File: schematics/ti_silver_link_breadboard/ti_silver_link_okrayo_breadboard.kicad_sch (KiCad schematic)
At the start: 35 parts, among them P1 USB_B, U1 24LC256, U2 MCP17003302E, U3 TUSB3410, U4A PN2222A, U4B PN2222A, Y1 12MHz

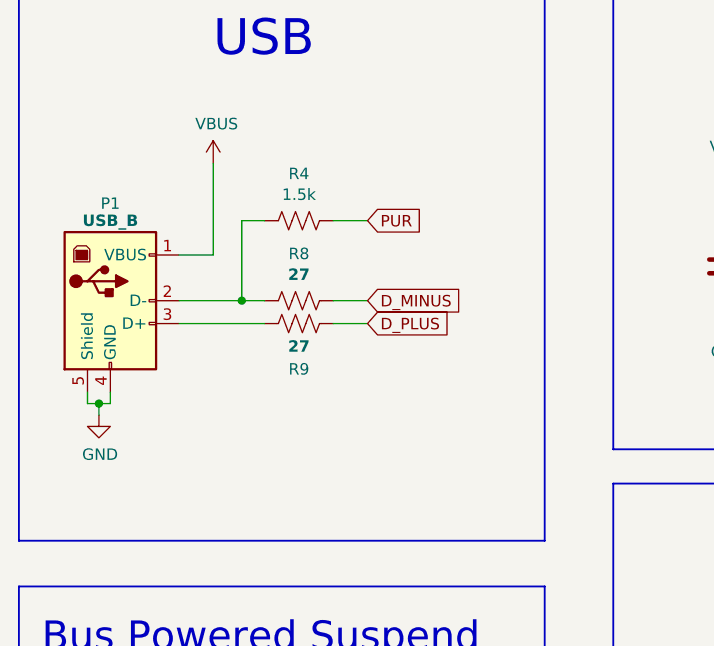
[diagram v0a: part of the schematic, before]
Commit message: Correct "B" and "okrayo" PUR resistor connection to D+
Rev 1 schematic incorrectly identified PUR resistor connection to D- and
had the series resistors for D+/D- (R8/R9) swapped. Move PUR resistor R4
to D+ and use R8 for D+ and R9 for D-.
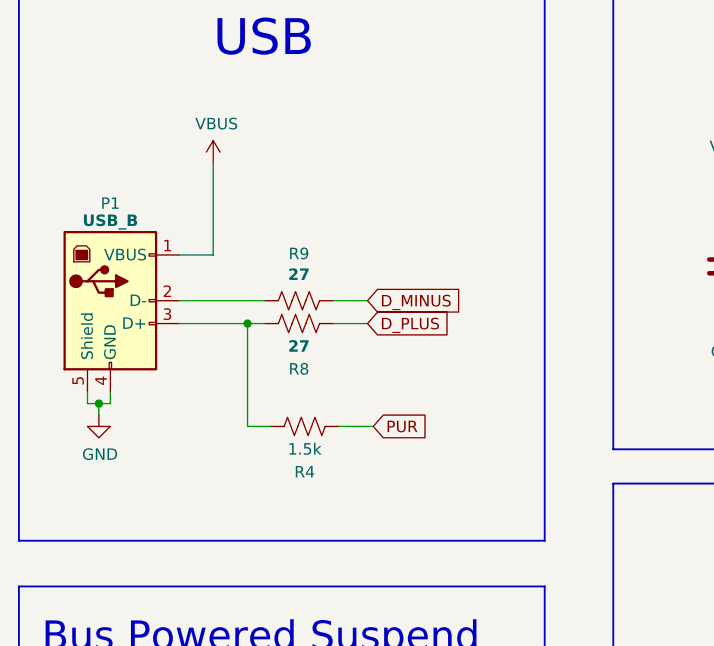
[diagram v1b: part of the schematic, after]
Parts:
- renumbered R9 to R8, R8 to R9
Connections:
- net at P1.2 (D-), R9.2: no longer R4.2
- net at P1.3 (D+), R8.2: now also R4.2
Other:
- moved on the sheet: R4
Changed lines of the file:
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@@
   (title_block
     (title "TI USB Graph Link \"okrayo\" Breadboard")
-    (date "2023-Jun-17")
-    (rev "1")
+    (date "2023-Jul-09")
+    (rev "2")
   )
   (junction (at 114.3 139.7) (diameter 0) (color 0 0 0 0)
@@
   (junction (at 135.89 44.45) (diameter 0) (color 0 0 0 0)
   )
+  (junction (at 60.96 57.15) (diameter 0) (color 0 0 0 0)
+  )
   (junction (at 44.45 66.04) (diameter 0) (color 0 0 0 0)
-  )
-  (junction (at 60.325 54.61) (diameter 0) (color 0 0 0 0)
   )
   (junction (at 64.77 118.11) (diameter 0) (color 0 0 0 0)
@@
     (stroke (width 0.2032) (type solid))
   )
-  (wire (pts (xy 70.485 45.72) (xy 74.295 45.72))
-    (stroke (width 0) (type default))
-  )
   (wire (pts (xy 233.68 83.82) (xy 233.68 85.09))
     (stroke (width 0) (type default))
@@
     (stroke (width 0) (type default))
   )
-  (wire (pts (xy 53.34 54.61) (xy 60.325 54.61))
+  (wire (pts (xy 53.34 54.61) (xy 62.865 54.61))
     (stroke (width 0) (type default))
   )
@@
     (stroke (width 0) (type default))
   )
-  (wire (pts (xy 60.325 45.72) (xy 60.325 54.61))
-    (stroke (width 0) (type default))
-  )
   (wire (pts (xy 135.89 54.61) (xy 135.89 55.88))
     (stroke (width 0) (type default))
@@
     (stroke (width 0) (type default))
   )
+  (wire (pts (xy 60.96 57.15) (xy 60.96 68.58))
+    (stroke (width 0) (type default))
+  )
   (wire (pts (xy 237.49 60.96) (xy 238.76 60.96))
     (stroke (width 0) (type default))
@@
     (stroke (width 0) (type default))
   )
-  (wire (pts (xy 60.325 54.61) (xy 62.865 54.61))
-    (stroke (width 0) (type default))
-  )
   (wire (pts (xy 154.94 40.64) (xy 154.94 39.37))
     (stroke (width 0) (type default))
@@
     (stroke (width 0.2032) (type solid))
   )
-  (wire (pts (xy 62.865 45.72) (xy 60.325 45.72))
+  (wire (pts (xy 63.5 68.58) (xy 60.96 68.58))
     (stroke (width 0) (type default))
   )
@@
     (stroke (width 0.2032) (type solid))
   )
+  (wire (pts (xy 60.96 57.15) (xy 62.865 57.15))
+    (stroke (width 0) (type default))
+  )
   (wire (pts (xy 70.485 57.15) (xy 74.295 57.15))
     (stroke (width 0) (type default))
@@
     (stroke (width 0) (type default))
   )
-  (wire (pts (xy 53.34 57.15) (xy 62.865 57.15))
+  (wire (pts (xy 53.34 57.15) (xy 60.96 57.15))
     (stroke (width 0) (type default))
   )
@@
   )
   (wire (pts (xy 154.94 92.71) (xy 154.94 91.44))
+    (stroke (width 0) (type default))
+  )
+  (wire (pts (xy 71.12 68.58) (xy 74.93 68.58))
     (stroke (width 0) (type default))
   )
@@
     )
   )
-  (global_label "PUR" (shape input) (at 74.295 45.72 0)
-    (effects (font (size 1.27 1.27)) (justify left))
-    (property "Intersheetrefs" "${INTERSHEET_REFS}" (at 74.295 45.72 0)
+  (global_label "PUR" (shape input) (at 74.93 68.58 0)
+    (effects (font (size 1.27 1.27)) (justify left))
+    (property "Intersheetrefs" "${INTERSHEET_REFS}" (at 74.93 68.58 0)
       (effects (font (size 1.27 1.27)) hide)
     )
@@
   (symbol (lib_id "Device:R_US") (at 66.675 54.61 270) (unit 1)
     (in_bom yes) (on_board yes) (dnp no)
-    (property "Reference" "R8" (at 66.675 49.403 90)
+    (property "Reference" "R9" (at 66.675 49.403 90)
       (effects (font (size 1.27 1.27)))
     )
@@
     )
     (property "Datasheet" "~" (at 66.675 54.61 0)
+      (effects (font (size 1.27 1.27)) hide)
+    )
+    (pin "1")
+    (pin "2")
+    (instances
+      (project "ti_silver_link_okrayo_breadboard"
+        (path "/683ce4bc-ff39-4a7c-bc2d-3e6ddc8eca85"
+          (reference "R9") (unit 1)
+        )
+      )
+    )
+  )
+  (symbol (lib_id "Device:R_US") (at 66.675 57.15 270) (unit 1)
+    (in_bom yes) (on_board yes) (dnp no)
+    (property "Reference" "R8" (at 66.675 62.23 90)
+      (effects (font (size 1.27 1.27)))
+    )
+    (property "Value" "27" (at 66.675 59.69 90)
+      (effects (font (size 1.27 1.27) bold))
+    )
+    (property "Footprint" "" (at 66.421 58.166 90)
+      (effects (font (size 1.27 1.27)) hide)
+    )
+    (property "Datasheet" "~" (at 66.675 57.15 0)
       (effects (font (size 1.27 1.27)) hide)
     )
@@
     )
   )
-  (symbol (lib_id "Device:R_US") (at 66.675 57.15 270) (unit 1)
-    (in_bom yes) (on_board yes) (dnp no)
-    (property "Reference" "R9" (at 66.675 62.23 90)
-      (effects (font (size 1.27 1.27)))
-    )
-    (property "Value" "27" (at 66.675 59.69 90)
-      (effects (font (size 1.27 1.27) bold))
-    )
-    (property "Footprint" "" (at 66.421 58.166 90)
-      (effects (font (size 1.27 1.27)) hide)
-    )
-    (property "Datasheet" "~" (at 66.675 57.15 0)
-      (effects (font (size 1.27 1.27)) hide)
-    )
-    (pin "1")
-    (pin "2")
-    (instances
-      (project "ti_silver_link_okrayo_breadboard"
-        (path "/683ce4bc-ff39-4a7c-bc2d-3e6ddc8eca85"
-          (reference "R9") (unit 1)
-        )
-      )
-    )
-  )
   (symbol (lib_id "Device:C") (at 135.89 50.8 0) (unit 1)
     (in_bom yes) (on_board yes) (dnp no)
@@
     )
   )
-  (symbol (lib_id "Device:R_US") (at 66.675 45.72 270) (unit 1)
-    (in_bom yes) (on_board yes) (dnp no)
-    (property "Reference" "R4" (at 66.675 40.513 90)
-      (effects (font (size 1.27 1.27)))
-    )
-    (property "Value" "1.5k" (at 66.675 42.8244 90)
-      (effects (font (size 1.27 1.27)))
-    )
-    (property "Footprint" "" (at 66.421 46.736 90)
-      (effects (font (size 1.27 1.27)) hide)
-    )
-    (property "Datasheet" "~" (at 66.675 45.72 0)
-      (effects (font (size 1.27 1.27)) hide)
-    )
+  (symbol (lib_id "Device:R_US") (at 67.31 68.58 270) (unit 1)
+    (in_bom yes) (on_board yes) (dnp no)
+    (property "Reference" "R4" (at 67.31 73.66 90)
+      (effects (font (size 1.27 1.27)))
+    )
+    (property "Value" "1.5k" (at 67.31 71.12 90)
+      (effects (font (size 1.27 1.27)))
+    )
+    (property "Footprint" "" (at 67.056 69.596 90)
+      (effects (font (size 1.27 1.27)) hide)
+    )
+    (property "Datasheet" "~" (at 67.31 68.58 0)
+      (effects (font (size 1.27 1.27)) hide)
+    )

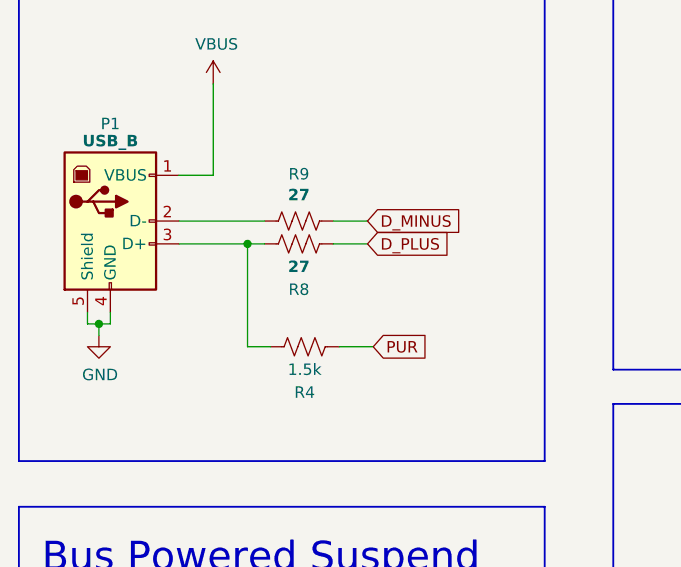
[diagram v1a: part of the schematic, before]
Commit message: Breadboard: move R4 D+ pullup resistor after R8 series resistor
TUSB3410 datasheet lists 1.5kΩ PUR pullup resistor after the D+ series
resistor. The USB Graph Link "B" schematic has this before the series
resistor. Correct "okrayo" breadboard schematic with this change to
align it with the datasheet.
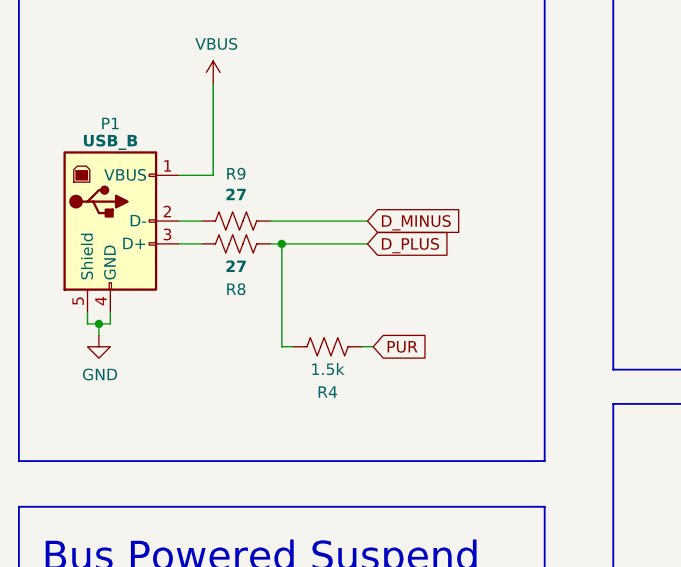
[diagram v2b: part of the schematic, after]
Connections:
- net D_PLUS: now also R4.2
- net at P1.3 (D+), R8.2: no longer R4.2
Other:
- moved on the sheet: R4, R8, R9
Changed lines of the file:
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@@
   (junction (at 238.76 60.96) (diameter 0) (color 0 0 0 0)
   )
+  (junction (at 64.77 57.15) (diameter 0) (color 0 0 0 0)
+  )
   (junction (at 215.9 127.635) (diameter 0) (color 0 0 0 0)
   )
@@
   )
   (junction (at 135.89 44.45) (diameter 0) (color 0 0 0 0)
-  )
-  (junction (at 60.96 57.15) (diameter 0) (color 0 0 0 0)
   )
   (junction (at 44.45 66.04) (diameter 0) (color 0 0 0 0)
@@
   (no_connect (at 175.26 132.08))
   (no_connect (at 175.26 124.46))
-  (wire (pts (xy 70.485 54.61) (xy 74.295 54.61))
+  (wire (pts (xy 63.5 54.61) (xy 74.295 54.61))
     (stroke (width 0) (type default))
   )
@@
     (stroke (width 0) (type default))
   )
+  (wire (pts (xy 64.77 57.15) (xy 74.295 57.15))
+    (stroke (width 0) (type default))
+  )
+  (wire (pts (xy 64.77 68.58) (xy 66.04 68.58))
+    (stroke (width 0) (type default))
+  )
   (wire (pts (xy 64.77 119.38) (xy 64.77 118.11))
     (stroke (width 0) (type default))
@@
     (stroke (width 0) (type default))
   )
+  (wire (pts (xy 64.77 57.15) (xy 64.77 68.58))
+    (stroke (width 0) (type default))
+  )
   (polyline (pts (xy 35.56 177.8) (xy 35.56 142.24))
     (stroke (width 0.2032) (type solid))
@@
     (stroke (width 0) (type default))
   )
-  (wire (pts (xy 53.34 54.61) (xy 62.865 54.61))
+  (wire (pts (xy 53.34 54.61) (xy 55.88 54.61))
     (stroke (width 0) (type default))
   )
@@
     (stroke (width 0) (type default))
   )
-  (wire (pts (xy 60.96 57.15) (xy 60.96 68.58))
-    (stroke (width 0) (type default))
-  )
   (wire (pts (xy 237.49 60.96) (xy 238.76 60.96))
     (stroke (width 0) (type default))
@@
     (stroke (width 0.2032) (type solid))
   )
-  (wire (pts (xy 63.5 68.58) (xy 60.96 68.58))
-    (stroke (width 0) (type default))
-  )
   (wire (pts (xy 217.17 125.095) (xy 215.9 125.095))
     (stroke (width 0) (type default))
@@
     (stroke (width 0.2032) (type solid))
   )
-  (wire (pts (xy 60.96 57.15) (xy 62.865 57.15))
-    (stroke (width 0) (type default))
-  )
-  (wire (pts (xy 70.485 57.15) (xy 74.295 57.15))
+  (wire (pts (xy 63.5 57.15) (xy 64.77 57.15))
     (stroke (width 0) (type default))
   )
@@
     (stroke (width 0) (type default))
   )
-  (wire (pts (xy 53.34 57.15) (xy 60.96 57.15))
+  (wire (pts (xy 53.34 57.15) (xy 55.88 57.15))
     (stroke (width 0) (type default))
   )
@@
     (stroke (width 0) (type default))
   )
-  (wire (pts (xy 71.12 68.58) (xy 74.93 68.58))
+  (wire (pts (xy 73.66 68.58) (xy 74.93 68.58))
     (stroke (width 0) (type default))
   )
@@
     )
   )
-  (symbol (lib_id "Device:R_US") (at 66.675 54.61 270) (unit 1)
-    (in_bom yes) (on_board yes) (dnp no)
-    (property "Reference" "R9" (at 66.675 49.403 90)
-      (effects (font (size 1.27 1.27)))
-    )
-    (property "Value" "27" (at 66.675 51.7144 90)
+  (symbol (lib_id "Device:R_US") (at 59.69 54.61 270) (unit 1)
+    (in_bom yes) (on_board yes) (dnp no)
+    (property "Reference" "R9" (at 59.69 49.403 90)
+      (effects (font (size 1.27 1.27)))
+    )
+    (property "Value" "27" (at 59.69 51.7144 90)
       (effects (font (size 1.27 1.27) bold))
     )
-    (property "Footprint" "" (at 66.421 55.626 90)
-      (effects (font (size 1.27 1.27)) hide)
-    )
-    (property "Datasheet" "~" (at 66.675 54.61 0)
+    (property "Footprint" "" (at 59.436 55.626 90)
+      (effects (font (size 1.27 1.27)) hide)
+    )
+    (property "Datasheet" "~" (at 59.69 54.61 0)
       (effects (font (size 1.27 1.27)) hide)
     )
@@
     )
   )
-  (symbol (lib_id "Device:R_US") (at 66.675 57.15 270) (unit 1)
-    (in_bom yes) (on_board yes) (dnp no)
-    (property "Reference" "R8" (at 66.675 62.23 90)
-      (effects (font (size 1.27 1.27)))
-    )
-    (property "Value" "27" (at 66.675 59.69 90)
+  (symbol (lib_id "Device:R_US") (at 59.69 57.15 270) (unit 1)
+    (in_bom yes) (on_board yes) (dnp no)
+    (property "Reference" "R8" (at 59.69 62.23 90)
+      (effects (font (size 1.27 1.27)))
+    )
+    (property "Value" "27" (at 59.69 59.69 90)
       (effects (font (size 1.27 1.27) bold))
     )
-    (property "Footprint" "" (at 66.421 58.166 90)
-      (effects (font (size 1.27 1.27)) hide)
-    )
-    (property "Datasheet" "~" (at 66.675 57.15 0)
+    (property "Footprint" "" (at 59.436 58.166 90)
+      (effects (font (size 1.27 1.27)) hide)
+    )
+    (property "Datasheet" "~" (at 59.69 57.15 0)
       (effects (font (size 1.27 1.27)) hide)
     )
@@
     )
   )
-  (symbol (lib_id "Device:R_US") (at 67.31 68.58 270) (unit 1)
-    (in_bom yes) (on_board yes) (dnp no)
-    (property "Reference" "R4" (at 67.31 73.66 90)
-      (effects (font (size 1.27 1.27)))
-    )
-    (property "Value" "1.5k" (at 67.31 71.12 90)
-      (effects (font (size 1.27 1.27)))
-    )
-    (property "Footprint" "" (at 67.056 69.596 90)
-      (effects (font (size 1.27 1.27)) hide)
-    )
-    (property "Datasheet" "~" (at 67.31 68.58 0)
-      (effects (font (size 1.27 1.27)) hide)
-    )
+  (symbol (lib_id "Device:R_US") (at 69.85 68.58 270) (unit 1)
+    (in_bom yes) (on_board yes) (dnp no)
+    (property "Reference" "R4" (at 69.85 73.66 90)
+      (effects (font (size 1.27 1.27)))
+    )
+    (property "Value" "1.5k" (at 69.85 71.12 90)
+      (effects (font (size 1.27 1.27)))
+    )
+    (property "Footprint" "" (at 69.596 69.596 90)
+      (effects (font (size 1.27 1.27)) hide)
+    )
+    (property "Datasheet" "~" (at 69.85 68.58 0)
+      (effects (font (size 1.27 1.27)) hide)
+    )

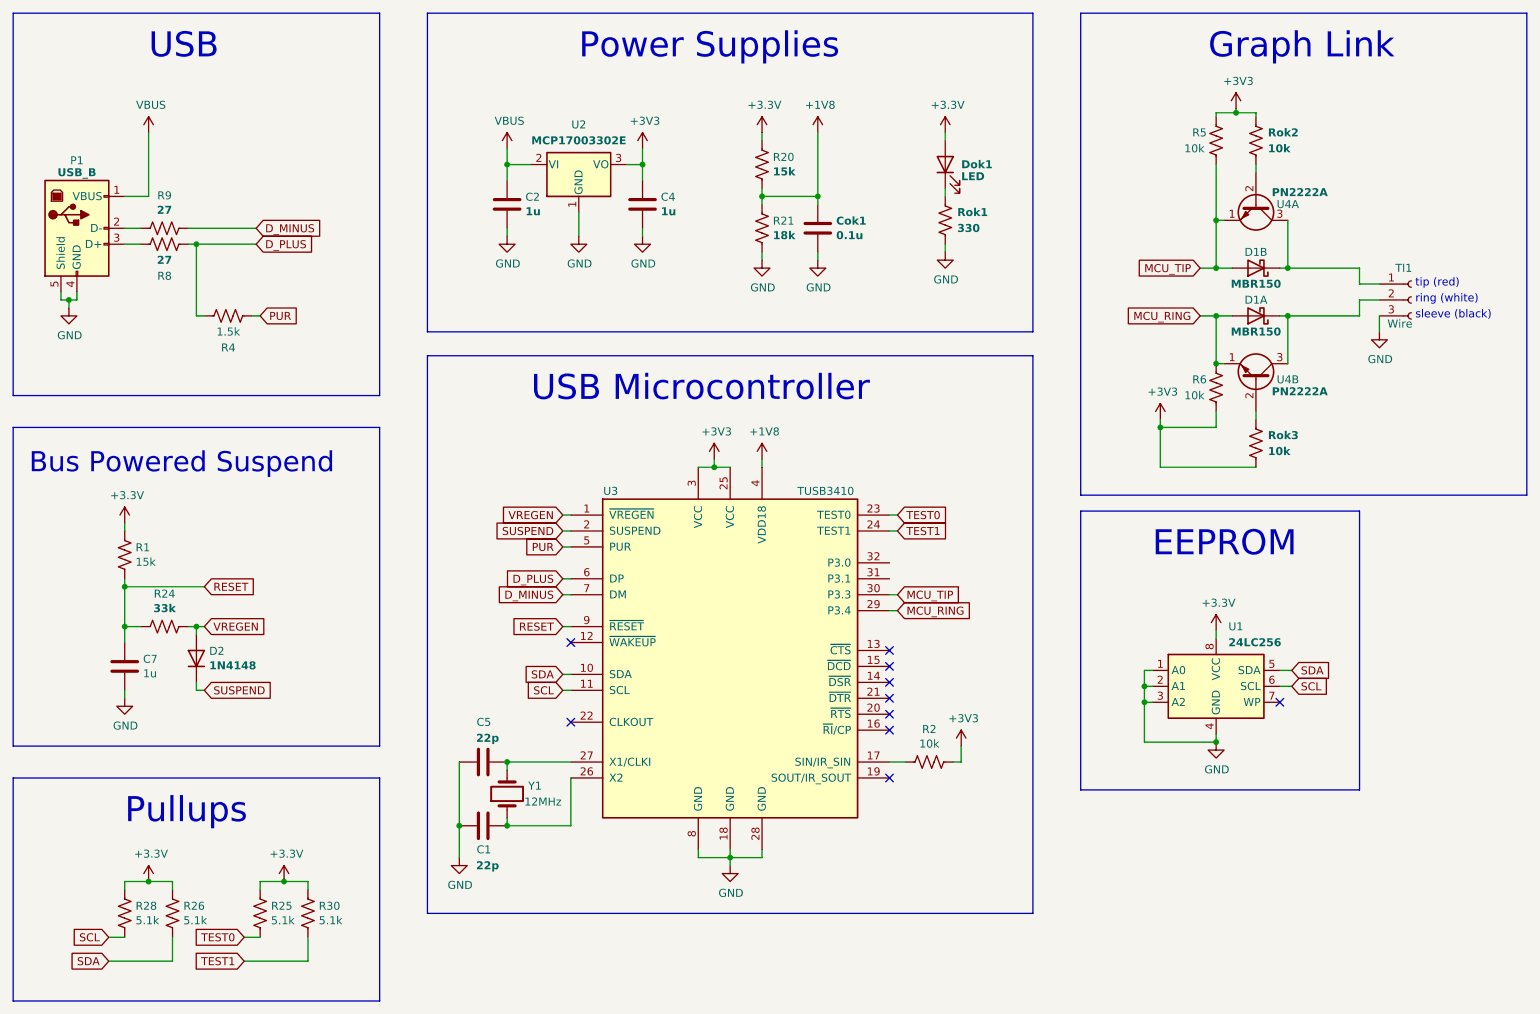
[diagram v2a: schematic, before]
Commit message: Convert all +3.3V nest to +3V3 in TI Silver Link "B" schematic
Addresses issue #3
USB Silver Link "B" schematic had a mix of +3.3V and +3V3 nets.
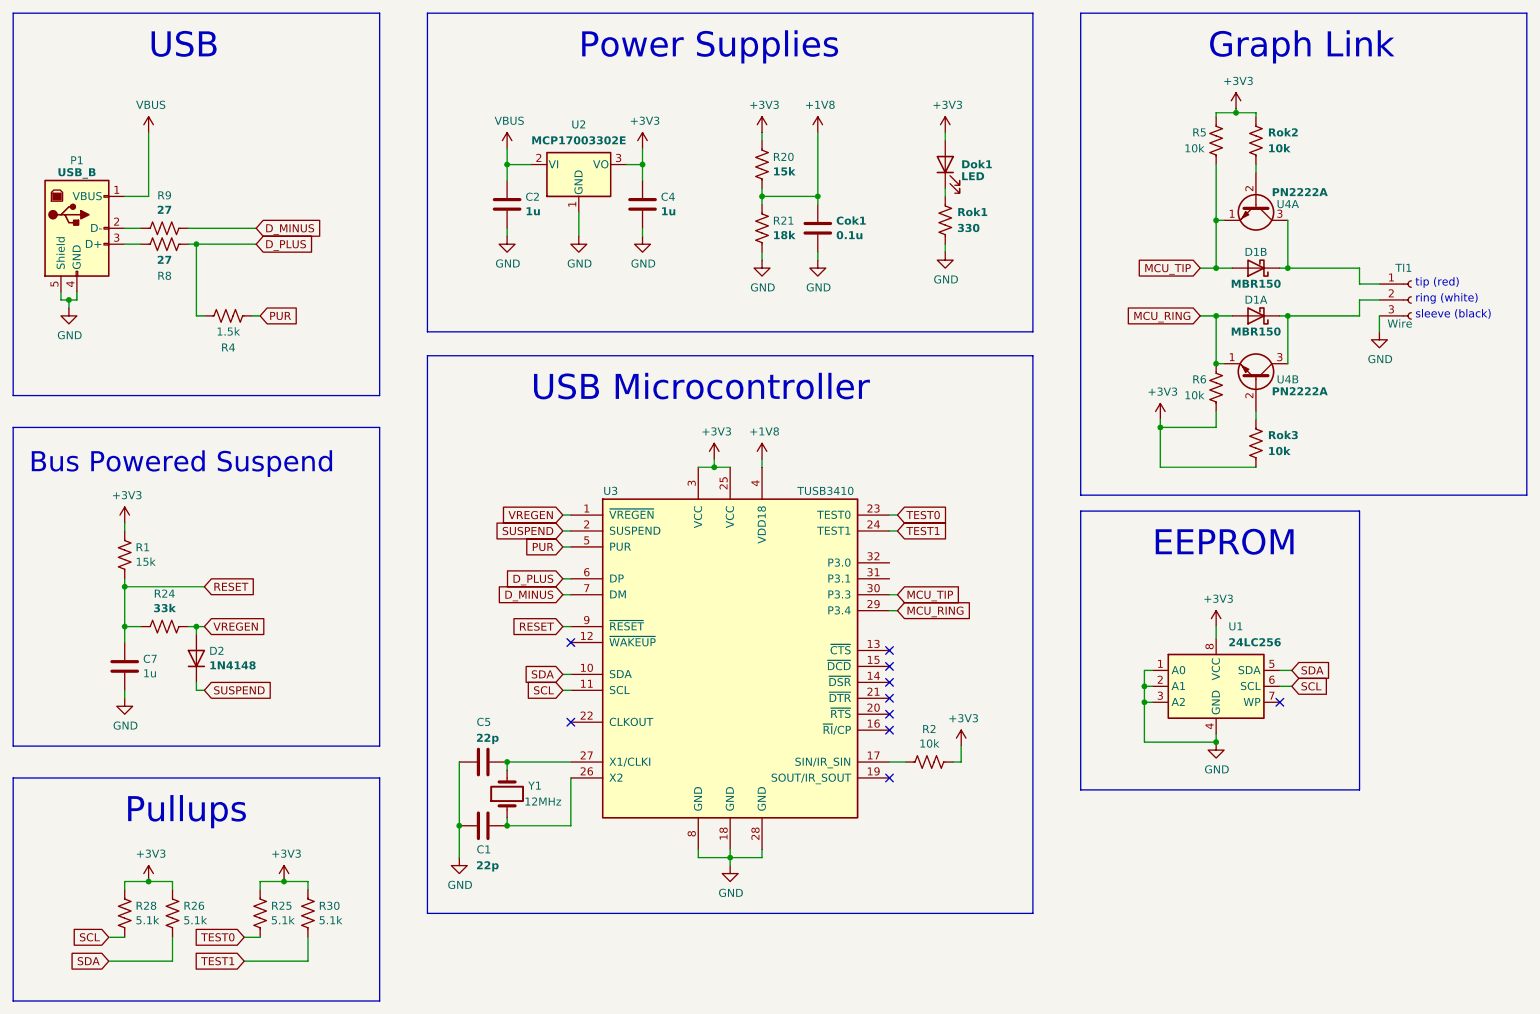
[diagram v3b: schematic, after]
